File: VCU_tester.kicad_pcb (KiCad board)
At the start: 2 copper layers, 200 x 172.5 mm, 112 parts, among them J1 Conn_01x04_Male, J10 DB9_Male, J11 DB9_Male, J12 Conn_01x08_Male, J13 Conn_01x08_Male, J14 USB_C_Receptacle, J15 USB_B_Micro, J2 Screw_Terminal_01x02, J3 DB9_Male, J4 DB9_Male, J5 DB9_Male, J500 Conn_01x10_Female, J501 Conn_01x08_Female, J502 Conn_01x08_Female, J503 Conn_01x08_Female, J504 Conn_01x08_Female, J505 Conn_01x08_Female, J507 Conn_02x18_Odd_Even, J6 DB9_Male, J7 Conn_01x04_Male, J8 DB9_Male, J9 DB9_Male, P8 BeagleBone_Black_Header, P9 BeagleBone_Black_Header, U1 REF3020, U2 MAX3232, U3 TCAN1042HVD, U4 MAX3232, U5 TCAN1042HVD, U6 DS3231MZ, U7 DS3231MZ

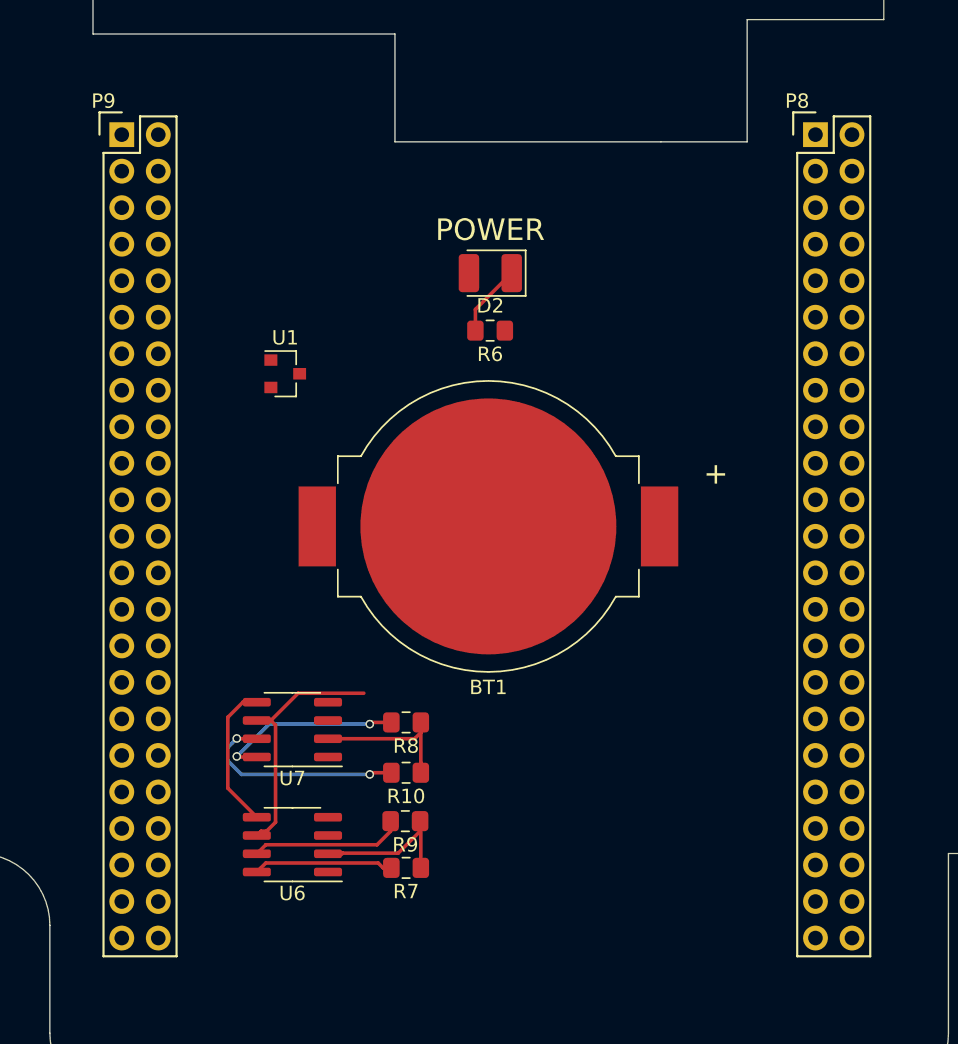
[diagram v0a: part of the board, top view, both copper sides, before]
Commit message: vcu & bb 3d models
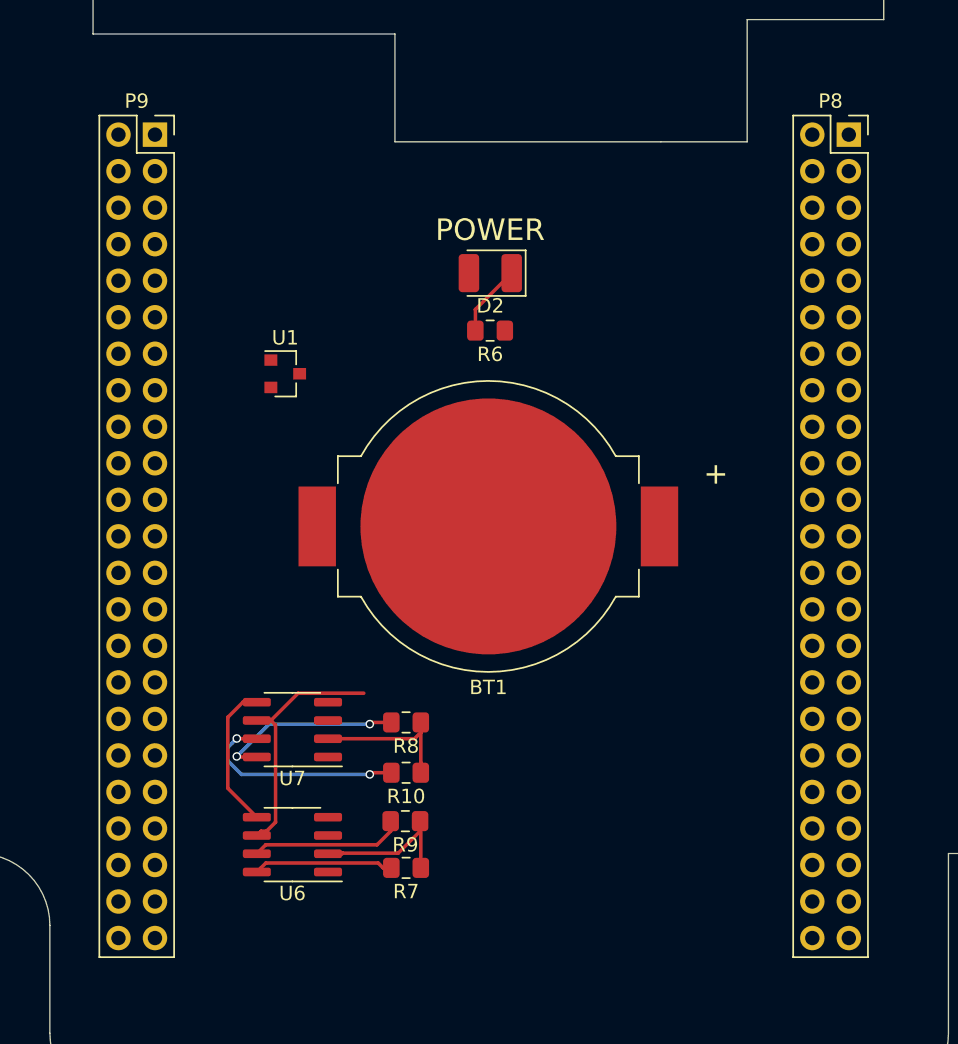
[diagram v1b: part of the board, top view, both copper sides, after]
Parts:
- removed the REF** at (65.0, 80.0)
- added REF**: BeagleBone-Black_Flip, project:BeagleBone-Black_Flip, F.Cu at (115.6, 80.0)
- P8, P9: footprint Socket_BeagleBone_Black:Socket_BeagleBone_Black -> project:PinHeader_2x23_P2.54mm_Vertical_Flip
- moved P8 2.32 mm to (115.6, 80.0)
- moved P9 2.31 mm to (67.3, 80.0)

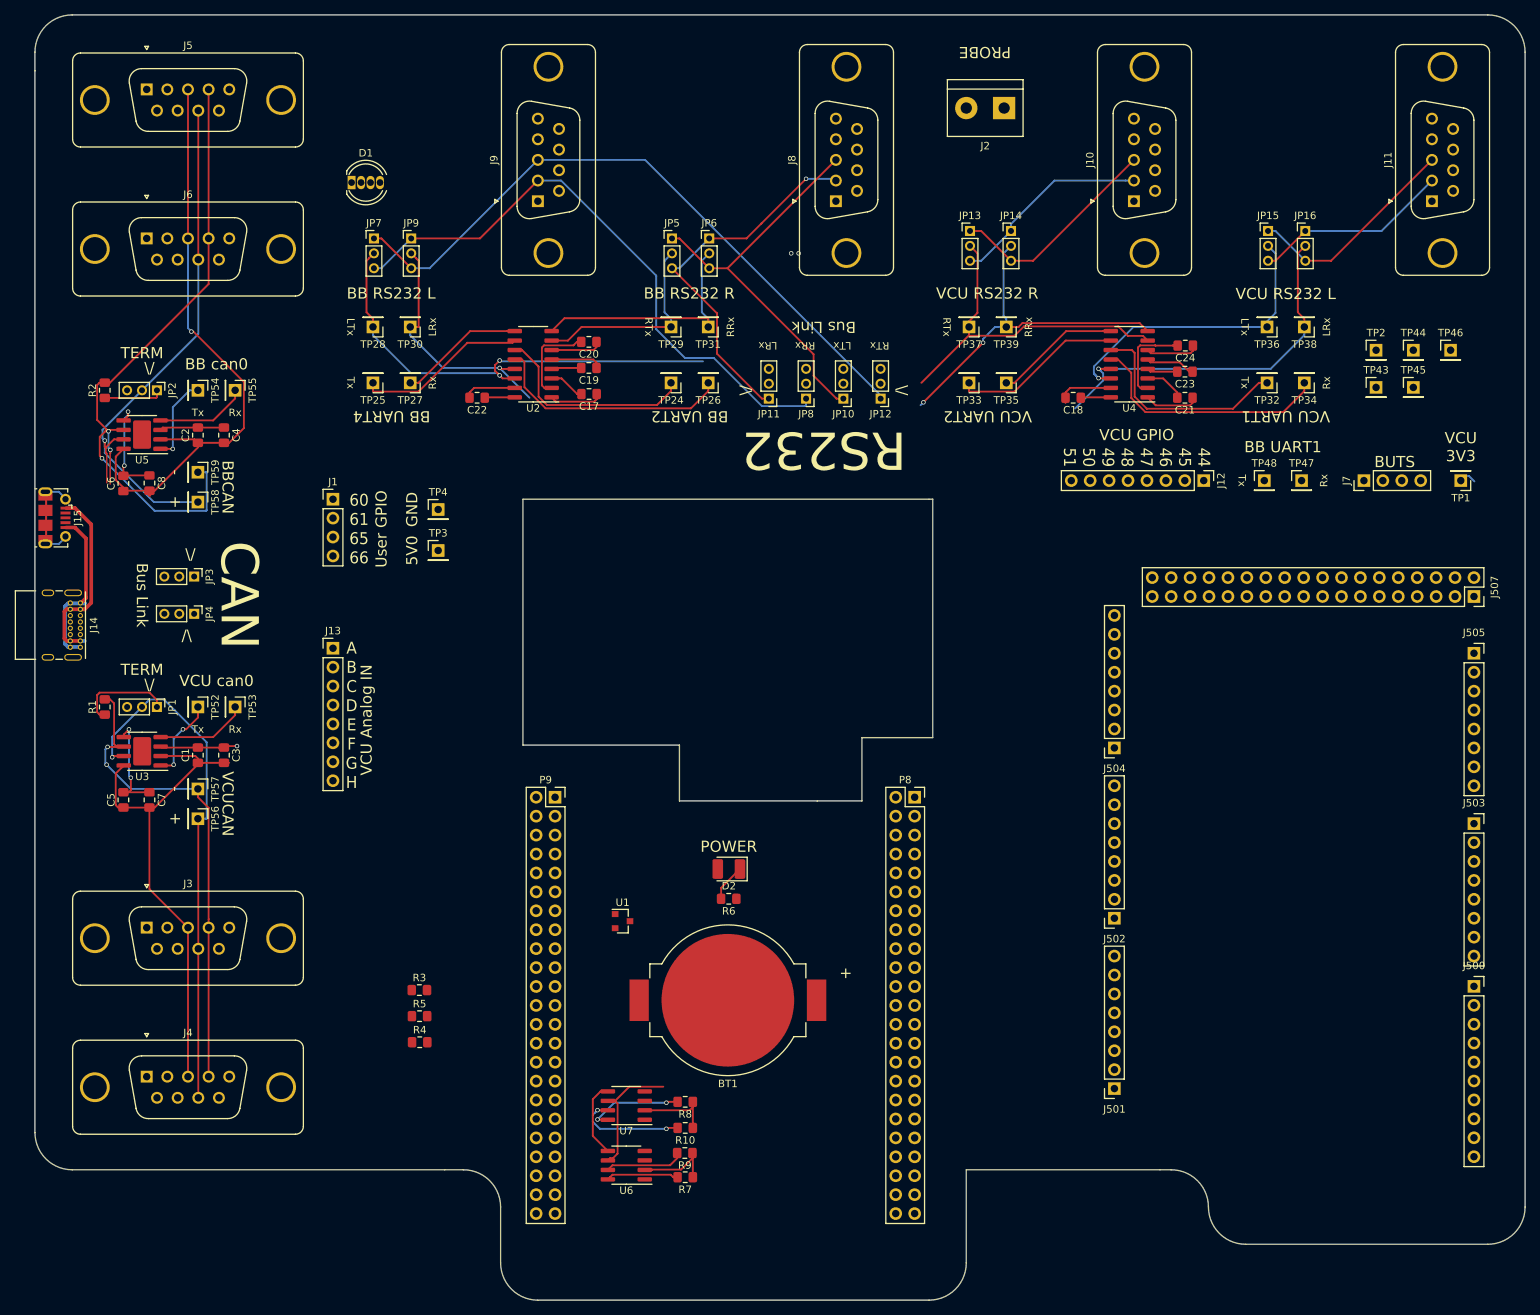
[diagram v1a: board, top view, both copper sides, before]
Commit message: Lots of layout, power bus
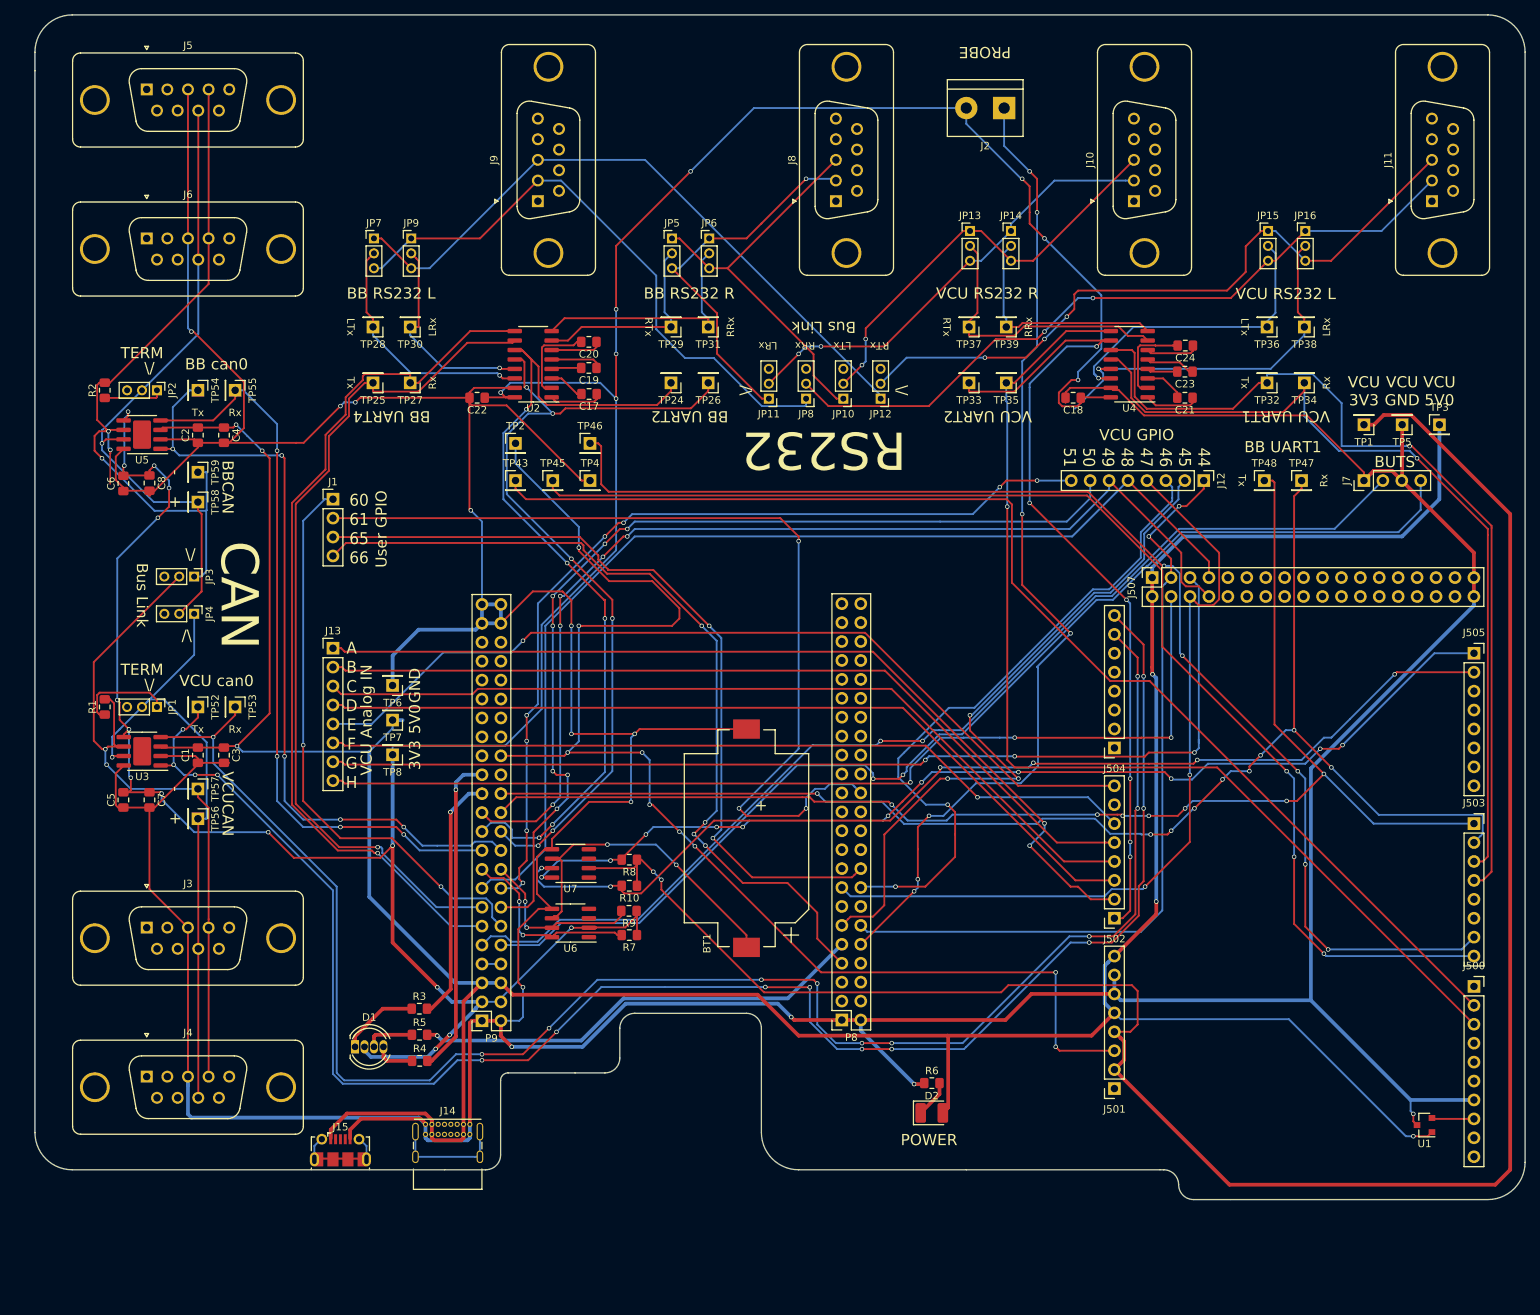
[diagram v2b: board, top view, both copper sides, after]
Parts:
- removed TP44: TestPoint, Connector_PinHeader_2.54mm:PinHeader_1x01_P2.54mm_Vertical
- added TP5: TestPoint, Connector_PinHeader_2.54mm:PinHeader_1x01_P2.54mm_Vertical, F.Cu at (181.0, 30.0)
- added TP6: TestPoint, Connector_PinHeader_2.54mm:PinHeader_1x01_P2.54mm_Vertical, F.Cu at (45.5, 65.0)
- added TP7: TestPoint, Connector_PinHeader_2.54mm:PinHeader_1x01_P2.54mm_Vertical, F.Cu at (45.5, 69.7)
- added TP8: TestPoint, Connector_PinHeader_2.54mm:PinHeader_1x01_P2.54mm_Vertical, F.Cu at (45.5, 74.3)
- BT1: footprint Battery:BatteryHolder_MPD_BC2003_1x2032 -> Battery:BatteryHolder_Keystone_1060_1x2032
- moved TP3 135.4 mm to (186.0, 30.0)
- moved TP2 116.2 mm to (62.0, 32.5)
- moved TP43 116.2 mm to (62.0, 37.5)
- moved TP45 116.2 mm to (67.0, 37.5)
- moved TP46 116.2 mm to (72.0, 32.5)
- moved D1 116.0 mm to (40.5, 113.5)
- moved U1 111.1 mm to (184.0, 124.0), turned to 180 degrees
- moved J15 93.1 mm to (38.5, 127.4), turned to 0 degrees
- moved J14 83.9 mm to (49.9, 123.9), turned to 0 degrees
- moved REF** 65.4 mm to (57.5, 110.0), turned to 180 degrees
- moved J507 43.3 mm to (147.4, 50.5), turned to 90 degrees
- moved D2 42.6 mm to (117.9, 122.4), turned to 0 degrees
- moved R6 36.8 mm to (117.9, 118.4), turned to 0 degrees
- moved R10 33.4 mm to (77.3, 91.9)
- moved R7 33.4 mm to (77.3, 98.5)
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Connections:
- net /AIR1 renamed Net-(J507-Pad32)
- net /AIR2 renamed Net-(J507-Pad30)
- net /AIR3 renamed Net-(J507-Pad29)
- net /GPIO_32 renamed /MMC1_DAT0
- net /GPIO_33 renamed /MMC1_DAT1
- net /GPIO_36 renamed /MMC1_DAT4
- net /GPIO_37 renamed /MMC1_DAT5
- net /GPIO_62 renamed /MMC1_CLK
- net /GPIO_63 renamed /MMC1_CMD
- net /MMC1_Dat2 renamed /MMC1_DAT2
- net /MMC1_Dat6 renamed /MMC1_DAT6
- net /MMC1_dat3 renamed /MMC1_DAT3
- net /MMC1_dat7 renamed /MMC1_DAT7
- net /PD27 renamed /TWD2
- net /PD28 renamed /TWCK2
- net /VCUCANRX1 renamed Net-(J507-Pad33)
- net /VCUGPIO_11 renamed Net-(J500-Pad4)
- net /VCUGPIO_12 renamed Net-(J500-Pad5)
- net /VCUGPIO_4 renamed Net-(J503-Pad5)
- net /VCUGPIO_5 renamed Net-(J503-Pad6)
- net /VCUGPIO_8 renamed Net-(J500-Pad1)
- net /VCUTXD1 renamed Net-(J507-Pad28)
- J500 pad 3: /VCUGPIO_10 -> /VCURXD2A
- J502 pad 1: /VCUGPIO_10 -> /VCUTXD2A
- J507 pad 10: /GPIO_51 -> Net-(J507-Pad10)
- J507 pad 27: /GPIO_22 -> Net-(J507-Pad27)
- J507 pad 31: /PressLin -> Net-(J507-Pad31)
- J507 pad 34: /PressLout -> Net-(J507-Pad34)
- J507 pad 4: /GPIO_45 -> /PressLout
- J507 pad 5: /GPIO_46 -> /PressLin
- J507 pad 9: /GPIO_50 -> Net-(J507-Pad9)
- P9 pad 17: /GPIO_5 -> /I2C1_SCL
- P9 pad 18: /GPIO_4 -> /I2C1_SDA
- R7 pad 2: /GPIO_4 -> /I2C1_SCL
- R9 pad 2: /GPIO_5 -> /I2C1_SDA
- TP33 pad 1: /VCUGPIO_10 -> /VCUTXD2A
- U4 pad 10: /VCUGPIO_10 -> /VCUTXD2A
- U6 pad 7: /GPIO_5 -> /I2C1_SDA
- U6 pad 8: /GPIO_4 -> /I2C1_SCL
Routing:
- net GNDD: track 196.0 -> 761.2 mm, vias 1 -> 13
- net +5V: track 44.2 -> 441.9 mm, vias 1 -> 6
- net +3V3: track 47.2 -> 422.2 mm, vias 4 -> 23
- net +3.3VA: track 13.3 -> 275.4 mm, vias 0 -> 2
- net /VCUCANTX0: track 11.1 -> 234.0 mm, vias 2 -> 13
- net /VCUCANRX0: track 12.3 -> 230.4 mm, vias 0 -> 10
- net /UART1_RXD: track 0.00 -> 183.7 mm, vias 0 -> 9
- net /UART1_TXD: track 0.00 -> 181.6 mm, vias 0 -> 7
- net /GPIO_112: track 0.00 -> 176.0 mm, vias 0 -> 9
- net /GPIO_7: track 0.00 -> 168.4 mm, vias 0 -> 5
- net /GPIO_5: track 10.7 -> 168.1 mm, vias 0 -> 3
- net /GPIO_4: track 9.75 -> 164.6 mm
- net SYS_RESETN: track 0.00 -> 153.8 mm, vias 0 -> 2
- net PWR_BUT: track 0.00 -> 147.4 mm, vias 0 -> 2
- net /GPIO_48: track 0.00 -> 144.5 mm
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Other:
- board size 200 x 172.5 mm -> 200 x 159 mm
- board text added: "3V3"
- board text added: "VCU 5V0"
- board text added: "VCU GND"

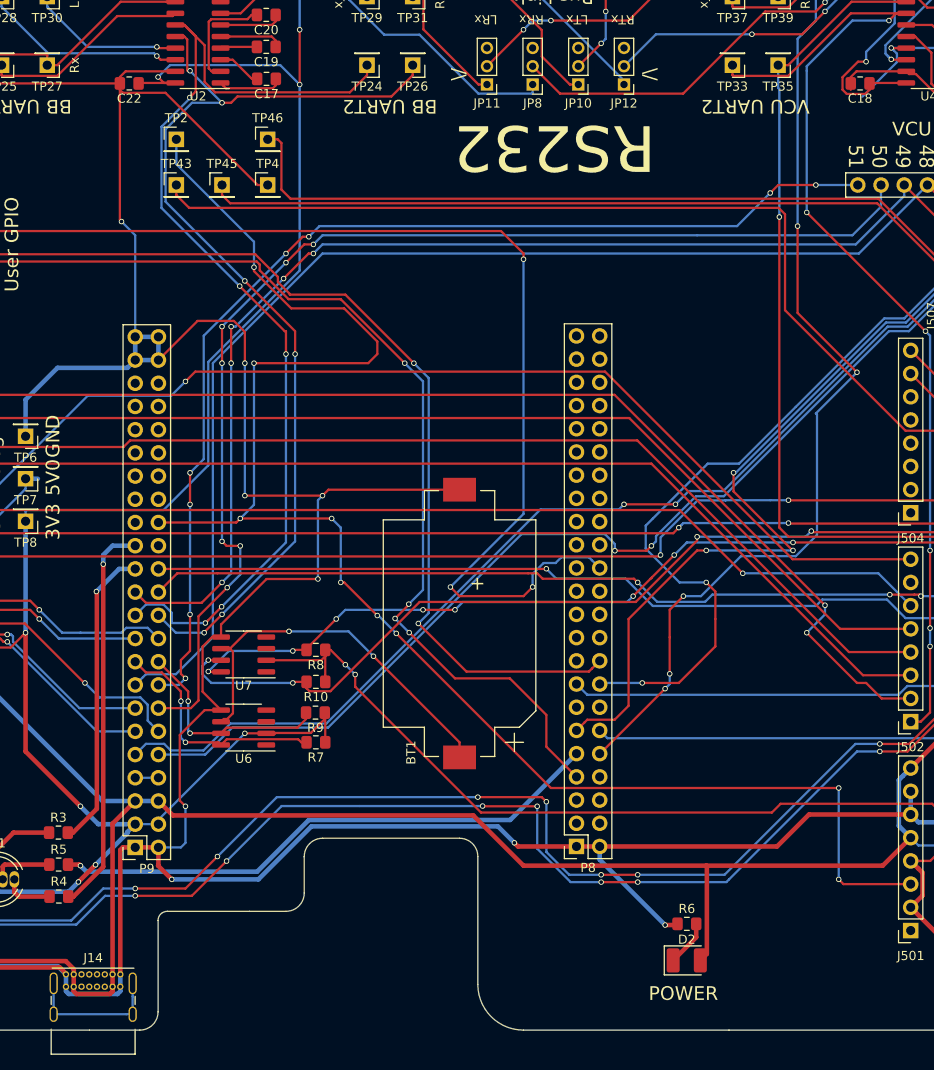
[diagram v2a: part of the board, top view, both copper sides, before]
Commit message: decouple caps, moved testpoint for usb access, tcan footprints
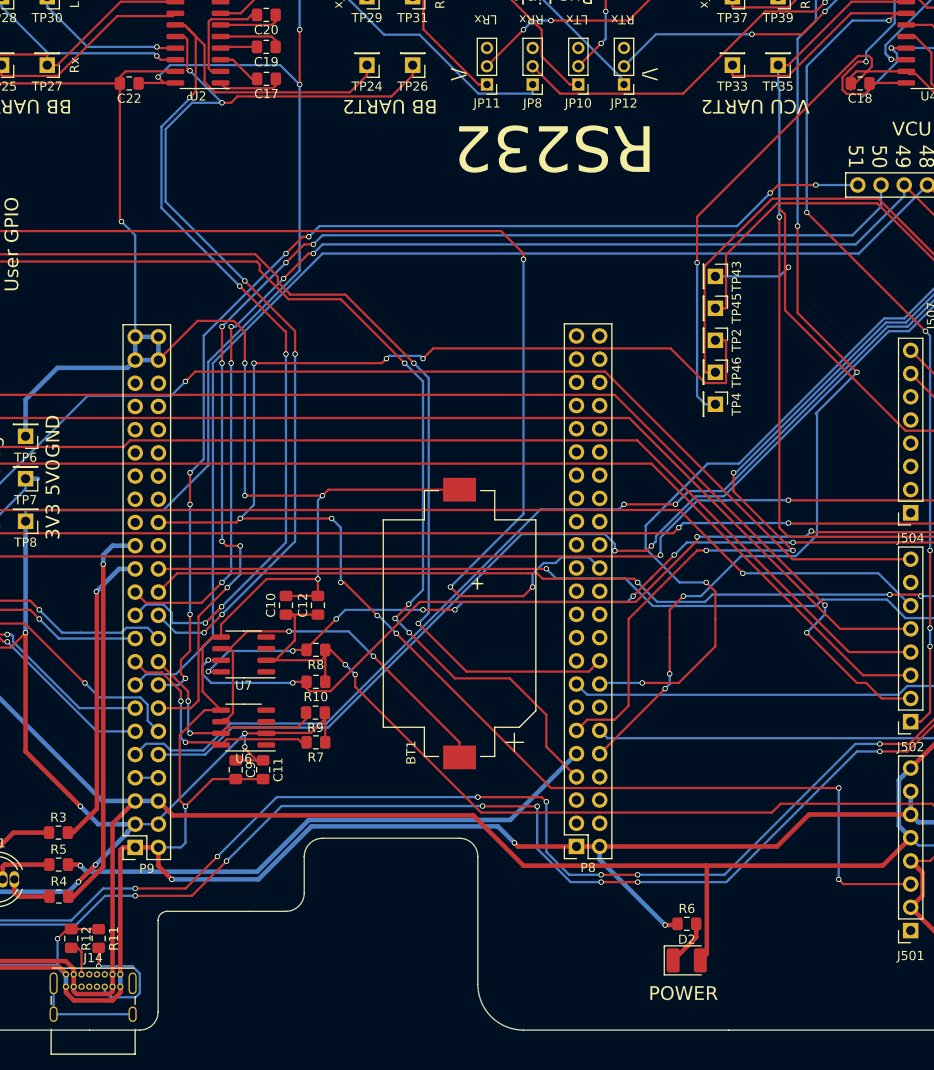
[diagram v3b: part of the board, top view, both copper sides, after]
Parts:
- added C10: 100p, Capacitor_SMD:C_0805_2012Metric_Pad1.15x1.40mm_HandSolder, F.Cu at (74.0, 83.5)
- added C11: 10n, Capacitor_SMD:C_0805_2012Metric_Pad1.15x1.40mm_HandSolder, F.Cu at (71.5, 101.5)
- added C12: 10n, Capacitor_SMD:C_0805_2012Metric_Pad1.15x1.40mm_HandSolder, F.Cu at (77.5, 83.5)
- added C9: 100p, Capacitor_SMD:C_0805_2012Metric_Pad1.15x1.40mm_HandSolder, F.Cu at (68.5, 101.5)
- added R11: 5K1, Resistor_SMD:R_0805_2012Metric_Pad1.15x1.40mm_HandSolder, F.Cu at (53.5, 120.0)
- added R12: 5K1, Resistor_SMD:R_0805_2012Metric_Pad1.15x1.40mm_HandSolder, F.Cu at (50.5, 120.0)
- moved TP2 63.0 mm to (121.0, 54.5), turned to 270 degrees
- moved TP43 59.8 mm to (121.0, 47.5), turned to 270 degrees
- moved TP45 55.7 mm to (121.0, 51.0), turned to 270 degrees
- moved TP46 55.2 mm to (121.0, 58.0), turned to 270 degrees
- moved TP4 54.6 mm to (121.0, 61.5), turned to 270 degrees
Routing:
- net /GPIO_4: track 164.6 -> 106.7 mm, vias 0 -> 1
- net GNDD: track 761.2 -> 817.0 mm, vias 13 -> 15
- net /GPIO_5: track 168.1 -> 120.8 mm
- net /GPIO_7: track 168.4 -> 130.7 mm
- net Net-(J14-PadB5): track 0.00 -> 13.8 mm, vias 0 -> 1
- net +3.3VA: track 275.4 -> 286.6 mm
- net /GPIO_112: track 176.0 -> 186.0 mm, vias 9 -> 10
- net +3V3: track 422.2 -> 429.4 mm, vias 23 -> 24
- net Net-(J14-PadA5): track 0.00 -> 3.77 mm
- net Net-(J14-PadS1): track 15.4 -> 12.0 mm
